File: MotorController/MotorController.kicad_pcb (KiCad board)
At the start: 2 copper layers, 30.5 x 17.8 mm, 17 parts, among them P1 MOTOR_2, P2 CONN_01X06, U1 L9110, U2 L9110

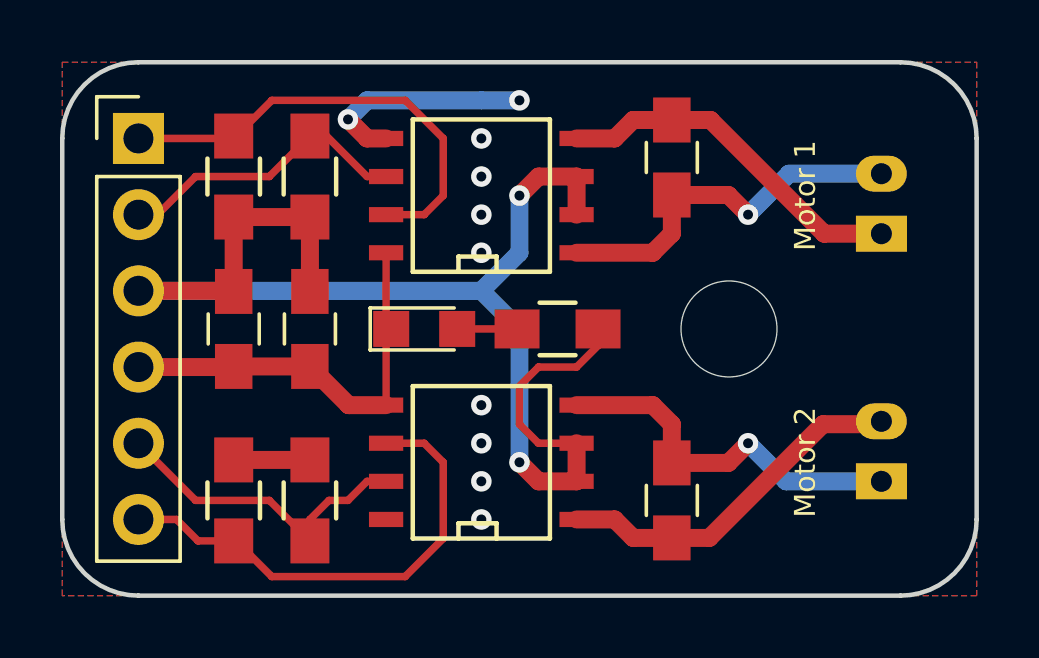
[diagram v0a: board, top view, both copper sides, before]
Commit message: Añadida serigrafia de pines, logo de MC y mandada a fabrica
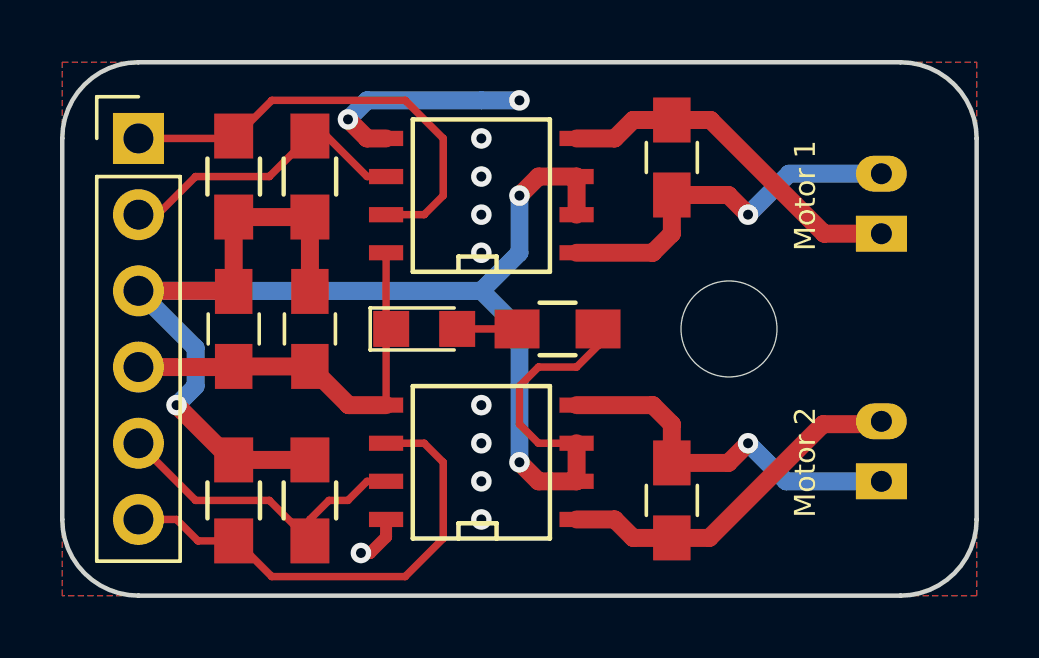
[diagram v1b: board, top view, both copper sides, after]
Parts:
- removed the G*** at (178.4, 86.4)
- added G***: LOGO, logos_frizzy:logo_mc, B.Cu at (174.8, 88.9)
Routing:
- net VCC: track 48.6 -> 56.2 mm, vias 2 -> 3
- net GND: track 22.8 -> 24.4 mm, vias 2 -> 3
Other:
- board text added: "GND"
- board text added: "M1-A"
- board text added: "M1-B"
- board text added: "M2-A"
- board text added: "M2-B"
- board text added: "VCC"
